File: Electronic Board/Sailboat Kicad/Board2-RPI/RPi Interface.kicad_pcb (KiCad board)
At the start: 2 copper layers, 69.9 x 99.1 mm, 18 parts, among them J1 Conn_01x06, J2 Conn_01x06, J23 Conn_02x20_Odd_Even, J25 Conn_01x03_Female, J26 Conn_01x03_Female, J27 Conn_01x03_Female, J28 Conn_01x03_Female, J29 Conn_01x03_Female, J3 Conn_02x02_Odd_Even, J30 Conn_01x03_Female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

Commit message: Hotfix on raspberry pi Card Radio interface
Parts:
- moved J25 15.2 mm to (139.1, 123.2)
- moved J4 15.2 mm to (139.1, 138.4)
- moved J26 10.2 mm to (139.1, 125.7)
- moved J30 10.2 mm to (139.1, 135.9)
- moved J27 5.08 mm to (139.1, 128.3)
- moved J29 5.08 mm to (139.1, 133.3)
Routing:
- net 5V-Sensors: track 238.1 -> 210.0 mm
- net RC_6: track 74.8 -> 91.9 mm
- net RC_1: track 76.3 -> 63.3 mm
- net RC_5: track 75.9 -> 85.6 mm
- net RC_2: track 76.3 -> 68.8 mm
- net RC_4: track 74.8 -> 80.0 mm
- net RC_3: track 75.9 -> 74.8 mm

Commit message: Hotfix again for Radio on Rasbperry pi
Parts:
- moved J30 8.26 mm to (139.1, 144.1)
- moved J26 8.26 mm to (139.1, 134.0)
- moved J25 8.25 mm to (139.1, 131.4)
- moved J27 8.25 mm to (139.1, 136.5)
- moved J28 8.25 mm to (139.1, 139.1)
- moved J29 8.25 mm to (139.1, 141.6)
- moved J4 8.25 mm to (139.1, 146.7)
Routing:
- net /Connectors/5V-RPi: track 140.5 -> 153.8 mm
- net RC_6: track 91.9 -> 100.1 mm
- net RC_2: track 68.8 -> 77.1 mm
- net RC_1: track 63.3 -> 71.5 mm
- net RC_5: track 85.6 -> 93.9 mm
- net RC_4: track 80.0 -> 88.3 mm
- net RC_3: track 74.8 -> 83.1 mm
- net GND: track 20.5 -> 28.8 mm
- net 5V-Sensors: track 210.0 -> 217.3 mm

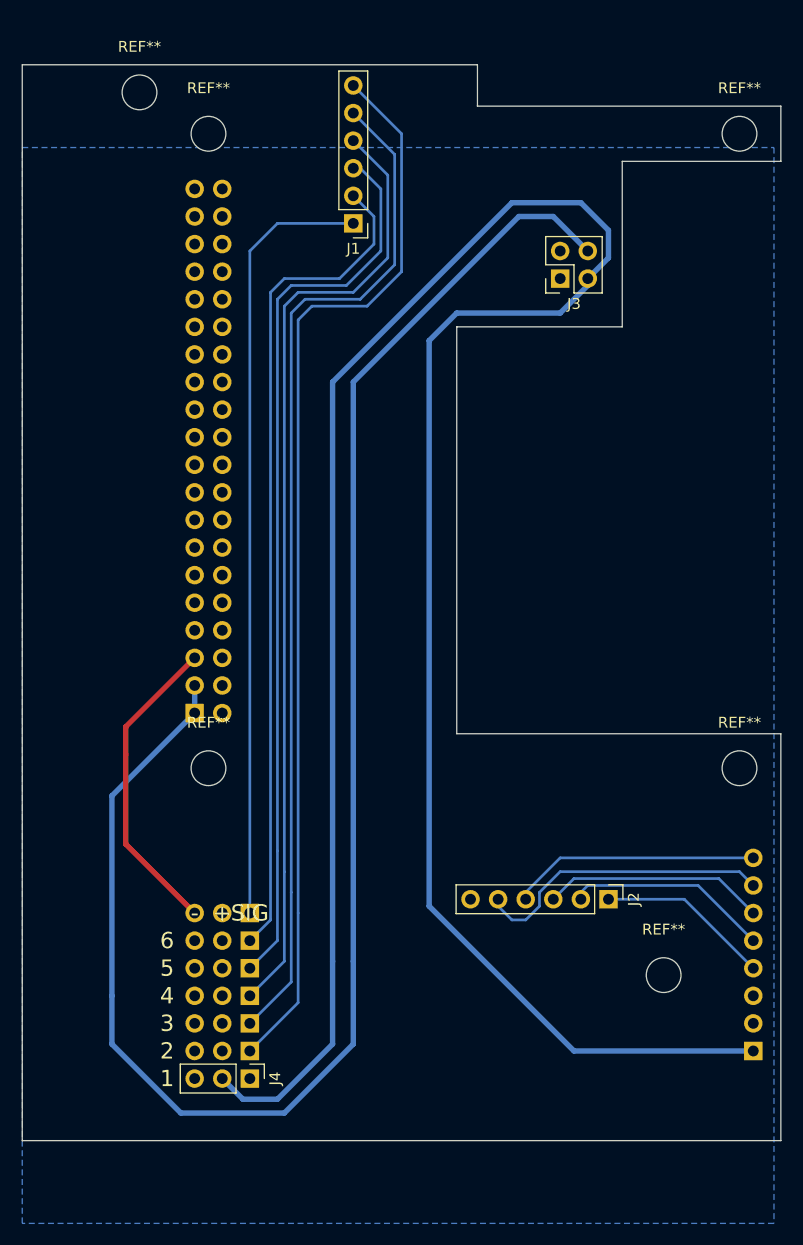
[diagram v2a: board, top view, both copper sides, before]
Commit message: Cleaned up, and added security, text and better usability, preparation for board v2
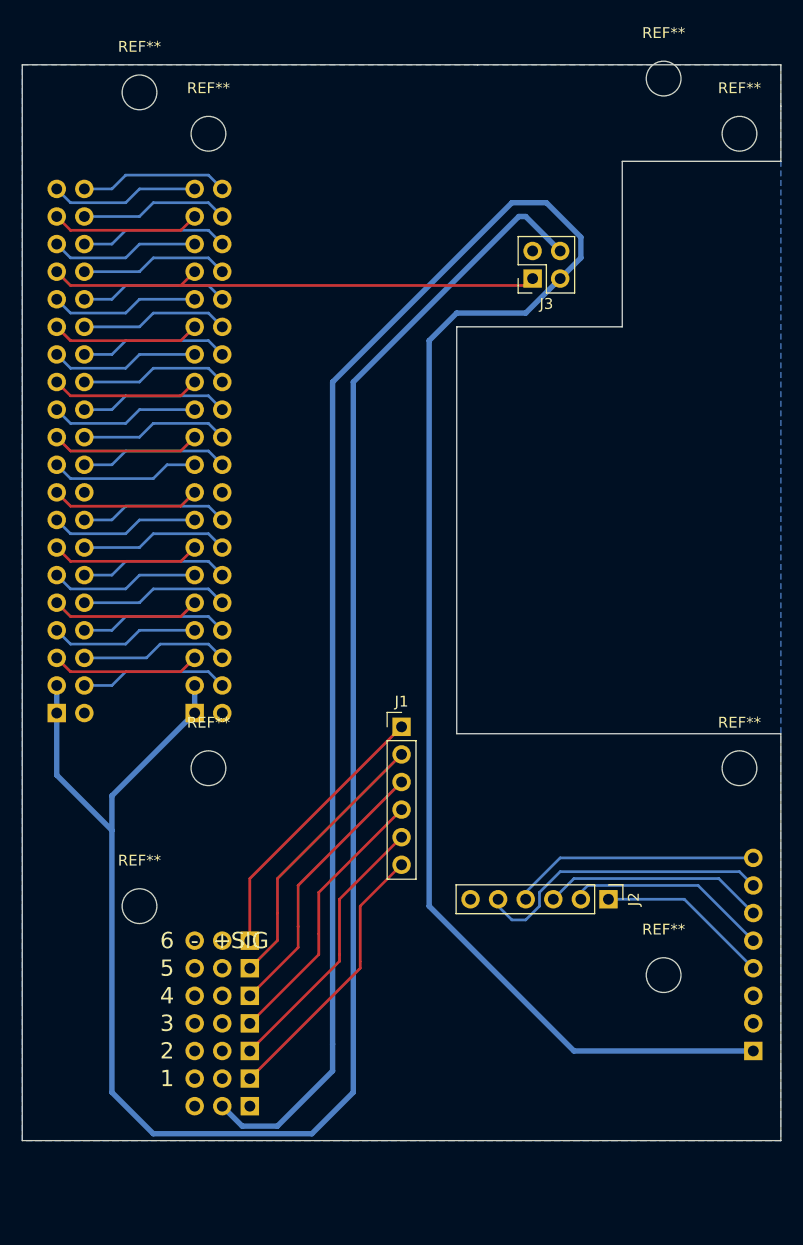
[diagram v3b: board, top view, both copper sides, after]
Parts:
- added J5: Conn_02x20_Odd_Even, Pin_Headers:Pin_Header_Straight_2x20_Pitch2.54mm, B.Cu at (121.3, 113.0)
- added REF**: MountingHole_3.2mm_M3, Mounting_Holes:MountingHole_3.2mm_M3, F.Cu at (128.9, 130.8)
- added REF**: MountingHole_3.2mm_M3, Mounting_Holes:MountingHole_3.2mm_M3, F.Cu at (177.2, 54.6)
- J4: moved to B.Cu
- moved J1 46.6 mm to (153.0, 114.3), turned to 0 degrees
- moved J25 2.54 mm to (139.1, 134.0)
- moved J29 2.54 mm to (139.1, 144.1)
- moved J26 2.54 mm to (139.1, 136.5)
- moved J27 2.54 mm to (139.1, 139.1)
- moved J28 2.54 mm to (139.1, 141.6)
- moved J3 2.54 mm to (165.1, 73.0)
- moved J30 2.54 mm to (139.1, 146.7)
- moved J4 2.54 mm to (139.1, 149.2), turned to 90 degrees
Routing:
- net GND: track 28.8 -> 142.7 mm
- net RC_6: track 100.1 -> 25.5 mm
- net RC_5: track 93.9 -> 25.5 mm
- net RC_4: track 88.3 -> 25.5 mm
- net RC_3: track 83.1 -> 25.5 mm
- net RC_2: track 77.1 -> 25.5 mm
- net RC_1: track 71.5 -> 25.5 mm
- net /Connectors/5V-RPi: track 153.8 -> 173.5 mm
- net /RPi/21_RPi: track 0.00 -> 13.8 mm
- net /RPi/16_RPi: track 0.00 -> 13.8 mm
- net /RPi/14_RPi: track 0.00 -> 13.8 mm
- net /RPi/25_RPi: track 0.00 -> 13.8 mm
- net /RPi/24_RPi: track 0.00 -> 13.8 mm
- net /RPi/ID_SD: track 0.00 -> 13.8 mm
- net /RPi/6_RPi: track 0.00 -> 13.8 mm
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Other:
- outline, holes or cut-outs redrawn
